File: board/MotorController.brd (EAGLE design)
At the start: 83.5 x 58.4 mm, 34 parts, among them Q1 IPP80P03P4L-04, Q2 8Mhz, T1 BT139X-600E, U1 ATTINY84-20PU

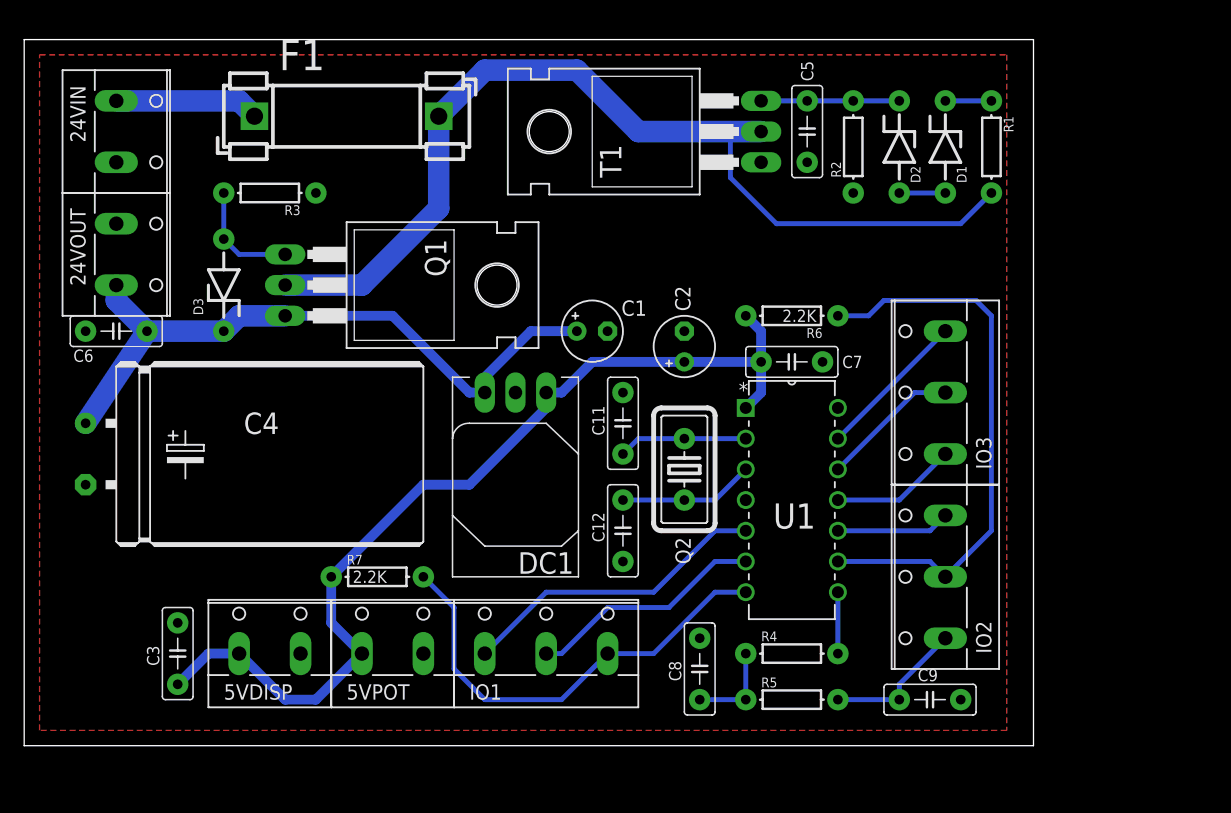
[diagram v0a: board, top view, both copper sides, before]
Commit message: Update with current design rules and current library
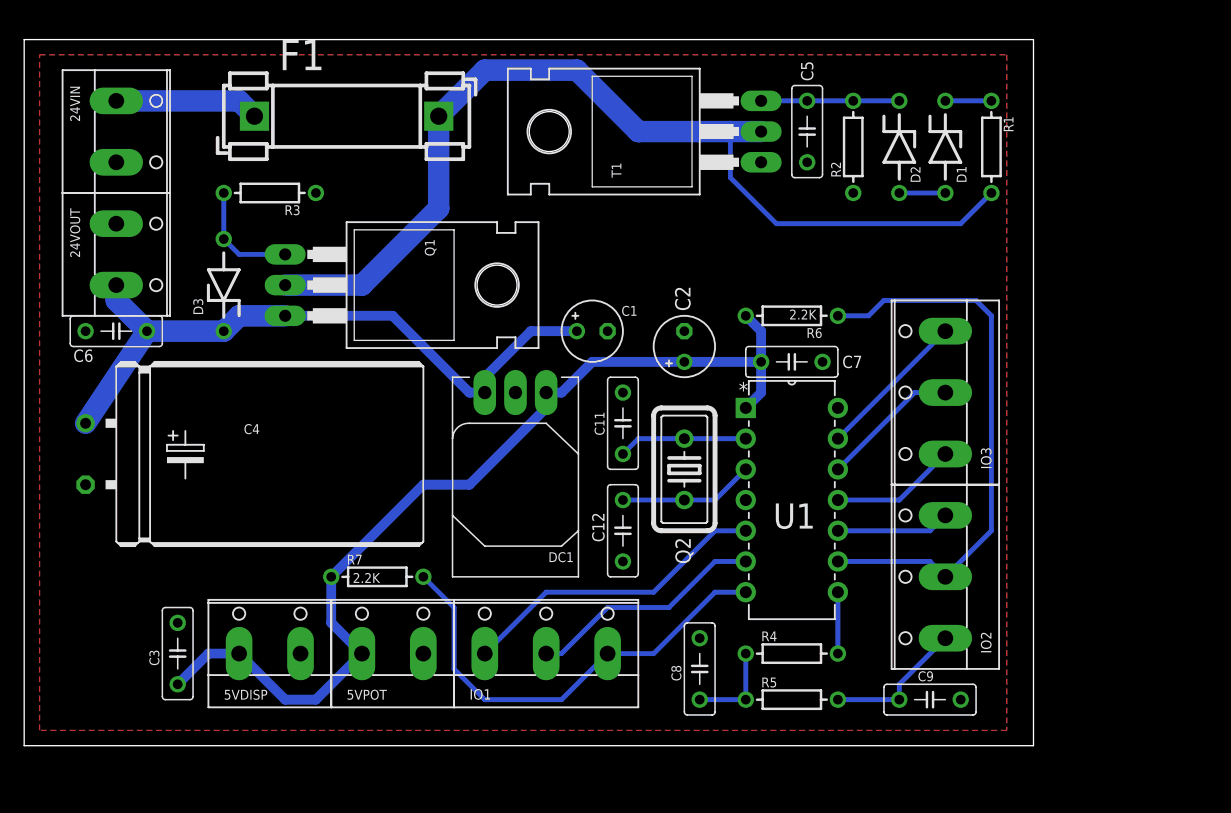
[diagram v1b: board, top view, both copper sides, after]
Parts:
- 24VIN, 24VOUT, 5VDISP, 5VPOT: value (none) -> SCREW-TERM-2
- C1, C2: device adafruit:E2,5-5 -> SaintGimp:CAP-POL-2.5-5
- F1: device fuse:FUSE_HOLDER_5X20MM -> SaintGimp:FUSE_HOLDER_5X20MM
- IO1, IO2, IO3: value (none) -> SCREW-TERM-3
- U1: device Atmel_By_element14_Batch_1:DIP254P762X533-14 -> SaintGimp:DIP14
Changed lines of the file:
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@@
 <?xml version="1.0" encoding="utf-8"?>
 <!DOCTYPE eagle SYSTEM "eagle.dtd">
-<eagle version="6.5.0">
+<eagle version="7.2.0">
 <drawing>
 <settings>
@@
 <layer number="56" name="wert" color="7" fill="1" visible="no" active="no"/>
 <layer number="57" name="tCAD" color="7" fill="1" visible="no" active="no"/>
+<layer number="90" name="Modules" color="5" fill="1" visible="no" active="no"/>
 <layer number="91" name="Nets" color="2" fill="1" visible="no" active="no"/>
 <layer number="92" name="Busses" color="1" fill="1" visible="no" active="no"/>
@@
 <layer number="97" name="Info" color="7" fill="1" visible="no" active="no"/>
 <layer number="98" name="Guide" color="6" fill="1" visible="no" active="no"/>
+<layer number="99" name="SpiceOrder" color="7" fill="1" visible="no" active="no"/>
 <layer number="100" name="Muster" color="7" fill="1" visible="no" active="no"/>
 <layer number="101" name="Patch_Top" color="12" fill="4" visible="no" active="yes"/>
@@
 <layer number="111" name="LPC17xx" color="7" fill="1" visible="yes" active="yes"/>
 <layer number="112" name="tSilk" color="7" fill="1" visible="yes" active="yes"/>
+<layer number="113" name="IDFDebug" color="7" fill="1" visible="yes" active="yes"/>
 <layer number="116" name="Patch_BOT" color="9" fill="4" visible="no" active="yes"/>
 <layer number="121" name="_tsilk" color="7" fill="1" visible="no" active="yes"/>
@@
 <layer number="223" name="223bmp" color="24" fill="1" visible="no" active="no"/>
 <layer number="224" name="224bmp" color="25" fill="1" visible="no" active="no"/>
+<layer number="225" name="225bmp" color="7" fill="1" visible="yes" active="yes"/>
+<layer number="226" name="226bmp" color="7" fill="1" visible="yes" active="yes"/>
+<layer number="227" name="227bmp" color="7" fill="1" visible="yes" active="yes"/>
+<layer number="228" name="228bmp" color="7" fill="1" visible="yes" active="yes"/>
+<layer number="229" name="229bmp" color="7" fill="1" visible="yes" active="yes"/>
+<layer number="230" name="230bmp" color="7" fill="1" visible="yes" active="yes"/>
+<layer number="231" name="231bmp" color="7" fill="1" visible="yes" active="yes"/>
 <layer number="248" name="Housing" color="7" fill="1" visible="yes" active="yes"/>
 <layer number="249" name="Edge" color="7" fill="1" visible="yes" active="yes"/>
@@
 <layer number="251" name="SMDround" color="12" fill="11" visible="no" active="no"/>
 <layer number="254" name="cooling" color="7" fill="1" visible="no" active="yes"/>
+<layer number="255" name="routoute" color="7" fill="1" visible="yes" active="yes"/>
 </layers>
 <board>
@@
 <param name="mdDrill" value="6mil"/>
 <param name="mdSmdStop" value="0mil"/>
-<param name="msWidth" value="6mil"/>
+<param name="msWidth" value="10mil"/>
 <param name="msDrill" value="13mil"/>
 <param name="msMicroVia" value="13mil"/>
 <param name="msBlindViaRatio" value="0.5"/>
-<param name="rvPadTop" value="0.25"/>
+<param name="rvPadTop" value="0.35"/>
 <param name="rvPadInner" value="0.25"/>
-<param name="rvPadBottom" value="0.25"/>
+<param name="rvPadBottom" value="0.35"/>
 <param name="rvViaOuter" value="0.25"/>
 <param name="rvViaInner" value="0.25"/>
@@
 <pass name="Default">
 <param name="RoutingGrid" value="8mil"/>
+<param name="AutoGrid" value="1"/>
+<param name="Efforts" value="0"/>
+<param name="TopRouterVariant" value="1"/>
 <param name="tpViaShape" value="round"/>
 <param name="PrefDir.1" value="0"/>
@@
 </autorouter>
 <elements>
-<element name="24VIN" library="SaintGimp" package="SCREW-TERM-2" value="" x="7.62" y="50.8" rot="R270"/>
-<element name="24VOUT" library="SaintGimp" package="SCREW-TERM-2" value="" x="7.62" y="40.64" rot="R270"/>
-<element name="5VPOT" library="SaintGimp" package="SCREW-TERM-2" value="" x="30.48" y="7.62"/>
-<element name="5VDISP" library="SaintGimp" package="SCREW-TERM-2" value="" x="20.32" y="7.62"/>
-<element name="C1" library="adafruit" package="E2,5-5" value="47uF" x="46.99" y="34.29"/>
+<element name="24VIN" library="SaintGimp" package="SCREW-TERM-2" value="SCREW-TERM-2" x="7.62" y="50.8" rot="R270"/>
+<element name="24VOUT" library="SaintGimp" package="SCREW-TERM-2" value="SCREW-TERM-2" x="7.62" y="40.64" rot="R270"/>
+<element name="5VPOT" library="SaintGimp" package="SCREW-TERM-2" value="SCREW-TERM-2" x="30.48" y="7.62"/>
+<element name="5VDISP" library="SaintGimp" package="SCREW-TERM-2" value="SCREW-TERM-2" x="20.32" y="7.62"/>
+<element name="C1" library="SaintGimp" package="CAP-POL-2.5-5" value="47uF" x="46.99" y="34.29"/>
 <element name="C4" library="SaintGimp" package="CAP-POL-25-14" value="470uF" x="22.86" y="24.13"/>
-<element name="F1" library="fuse" package="FUSE_HOLDER_5X20MM" value="FUSEBLANK_5X20MM" x="19.05" y="52.07">
-<attribute name="OC_NEWARK" value="unknown" x="19.05" y="52.07" size="1.778" layer="27" display="off"/>
-<attribute name="MPN" value="" x="19.05" y="52.07" size="1.778" layer="27" display="off"/>
-<attribute name="MF" value="" x="19.05" y="52.07" size="1.778" layer="27" display="off"/>
-<attribute name="OC_FARNELL" value="unknown" x="19.05" y="52.07" size="1.778" layer="27" display="off"/>
-</element>
+<element name="F1" library="SaintGimp" package="FUSE_HOLDER_5X20MM" value="FUSEBLANK_5X20MM" x="19.05" y="52.07"/>
 <element name="T1" library="SaintGimp" package="TO220BH" value="BT139X-600E" x="54.61" y="50.8" rot="R90"/>
 <element name="D2" library="SaintGimp" package="ZDIO-7.5" value="22V" x="72.39" y="49.53" smashed="yes" rot="R270">
@@
 </element>
 <element name="D3" library="SaintGimp" package="ZDIO-7.5" value="5.1V" x="16.51" y="38.1" rot="R90"/>
-<element name="C2" library="adafruit" package="E2,5-5" value="47uF" x="54.61" y="33.02" smashed="yes" rot="R90">
+<element name="C2" library="SaintGimp" package="CAP-POL-2.5-5" value="47uF" x="54.61" y="33.02" smashed="yes" rot="R90">
 <attribute name="NAME" x="55.118" y="35.941" size="1.27" layer="25" ratio="10" rot="R90"/>
 <attribute name="VALUE" x="57.023" y="35.433" size="1.27" layer="27" ratio="10" rot="R90"/>
@@
 <attribute name="VALUE" x="5.715" y="31.75" size="1.016" layer="27"/>
 </element>
-<element name="U1" library="Atmel_By_element14_Batch_1" package="DIP254P762X533-14" value="ATTINY84-20PU" x="67.31" y="12.7" smashed="yes">
+<element name="U1" library="SaintGimp" package="DIP14" value="ATTINY84-20PU" x="67.31" y="12.7" smashed="yes">
 <attribute name="PACKAGE" value="PDIP-14" x="41.91" y="43.18" size="1.778" layer="27" display="off"/>
 <attribute name="OC_NEWARK" value="58M3794" x="41.91" y="43.18" size="1.778" layer="27" display="off"/>
@@
 <attribute name="VALUE" value="" x="63.5" y="3.81" size="1.778" layer="27" display="off"/>
 </element>
-<element name="IO2" library="SaintGimp" package="SCREW-TERM-3" value="" x="76.2" y="13.97" rot="R90"/>
-<element name="IO3" library="SaintGimp" package="SCREW-TERM-3" value="" x="76.2" y="29.21" rot="R90"/>
-<element name="IO1" library="SaintGimp" package="SCREW-TERM-3" value="" x="43.18" y="7.62"/>
+<element name="IO2" library="SaintGimp" package="SCREW-TERM-3" value="SCREW-TERM-3" x="76.2" y="13.97" rot="R90"/>
+<element name="IO3" library="SaintGimp" package="SCREW-TERM-3" value="SCREW-TERM-3" x="76.2" y="29.21" rot="R90"/>
+<element name="IO1" library="SaintGimp" package="SCREW-TERM-3" value="SCREW-TERM-3" x="43.18" y="7.62"/>
 <element name="C8" library="SaintGimp" package="CAPACITOR-5MM" value="1uF" x="55.88" y="6.35" rot="R90"/>
 <element name="C9" library="SaintGimp" package="CAPACITOR-5MM" value="1uF" x="74.93" y="3.81"/>

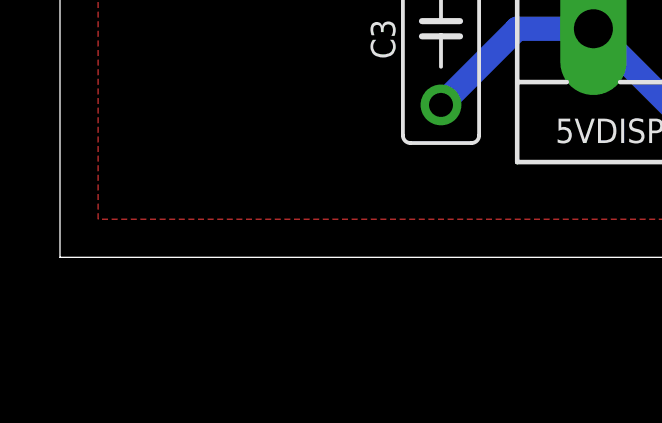
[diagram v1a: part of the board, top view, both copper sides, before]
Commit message: Pull up reset line
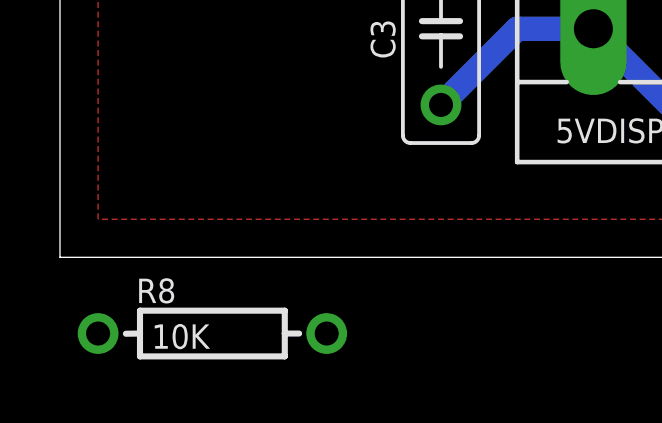
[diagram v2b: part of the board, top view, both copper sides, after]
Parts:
- added R8: 10K, SaintGimp:AXIAL-7.5MM
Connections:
- new net N$2: R8.P$2, U1.4
- new net VCC: R8.P$1
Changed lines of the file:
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@@
 <element name="R6" library="SaintGimp" package="AXIAL-7.5MM" value="2.2K" x="63.5" y="35.56" rot="R180"/>
 <element name="R7" library="SaintGimp" package="AXIAL-7.5MM" value="2.2K" x="29.21" y="13.97"/>
+<element name="R8" library="SaintGimp" package="AXIAL-7.5MM" value="10K" x="5.08" y="-2.54"/>
 </elements>
 <signals>
@@
 <wire x1="59.69" y1="3.81" x2="55.88" y2="3.81" width="0.4064" layer="16"/>
 </signal>
+<signal name="N$2">
+<contactref element="U1" pad="4"/>
+<contactref element="R8" pad="P$2"/>
+<wire x1="8.89" y1="-2.54" x2="59.69" y2="20.32" width="0" layer="19" extent="1-1"/>
+</signal>
+<signal name="VCC">
+<contactref element="R8" pad="P$1"/>
+</signal>
 </signals>

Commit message: New board layout
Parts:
- removed 5VDISP, 5VPOT: SCREW-TERM-2, SaintGimp:SCREW-TERM-2
- removed IO1, IO2, IO3: SCREW-TERM-3, SaintGimp:SCREW-TERM-3
- removed R7: 2.2K, SaintGimp:AXIAL-7.5MM
- added C10: 0.1uF, SaintGimp:CAPACITOR-5MM
- added CNTRL: SCREW-TERM-2, SaintGimp:SCREW-TERM-2
- added DISP, MOTOR, RAMP, SPD: SCREW-TERM-3, SaintGimp:SCREW-TERM-3
- added U$1, U$2, U$3, U$4: (no value), holes:4,1
- C11, C12: device SaintGimp:CAPACITOR-5MM -> SaintGimp:CAPACITOR-2.5MM
- C6: value 0.1uF -> 1uF
- F1: value FUSEBLANK_5X20MM -> 4A
- R1, R2: value 1K -> (none)
- R3, R8: value 10K -> (none)
- R4, R5: value 220 -> (none)
- R6: value 2.2K -> (none)
- moved 24VOUT 83.9 mm to (90.2, 25.4), turned to 90 degrees
- moved C6 74.9 mm to (82.5, 34.3), turned to 270 degrees
- moved C4 56.1 mm to (77.5, 11.4), turned to 270 degrees
- moved C3 55.4 mm to (64.8, 26.7), turned to 180 degrees
- moved R1 49.8 mm to (63.5, 2.54), turned to 180 degrees
- moved C7 48.4 mm to (15.2, 35.6), turned to 270 degrees
- moved F1 47.1 mm to (21.6, 5.08)
- moved D1 45.0 mm to (63.5, 6.35), turned to 180 degrees
- moved T1 44.7 mm to (49.5, 6.35)
- moved C9 43.1 mm to (45.7, 35.6), turned to 270 degrees
- moved R8 43.1 mm to (36.8, 26.7), turned to 180 degrees
- moved U1 42.4 mm to (34.3, 39.4), turned to 90 degrees
- moved D2 40.4 mm to (63.5, 10.2), turned to 180 degrees
- moved R6 38.6 mm to (25.4, 41.9), turned to 0 degrees
- moved R4 37.8 mm to (38.1, 35.6), turned to 90 degrees
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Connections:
- removed net 5V: 5VDISP.1, 5VPOT.1, C2.+, C3.1, C7.2, DC1.P3, R6.P$2, R7.P$1, U1.1
- removed net I2C_SCL: IO2.2, R6.P$1, U1.9
- removed net I2C_SDA: IO1.3, R7.P$2, U1.7
- new net N$8: DISP.3, R6.P$1
- new net SERIAL_TX: R6.P$2, U1.7
- net 24V-PROTECTED: now also C10.2
- net DIR_IN: now also CNTRL.1; no longer IO3.1
- net DIR_OUT: now also MOTOR.3; no longer IO1.2
- net GND: now also C10.1, DISP.2, RAMP.2, SPD.2; no longer 5VDISP.2, 5VPOT.2
- net N$10: now also MOTOR.1; no longer IO2.1
- net RAMP_IN: now also RAMP.3; no longer IO3.2
- net RPM_IN: now also MOTOR.2; no longer IO1.1
- net SPD_IN: now also SPD.3; no longer IO3.3
- net START_IN: now also CNTRL.2; no longer IO2.3
- net VCC: now also C2.+, C3.1, C7.2, DC1.P3, DISP.1, RAMP.1, SPD.1, U1.1
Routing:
- net VCC: track 0.00 -> 109.8 mm
- net 5V: track 79.2 -> 0.00 mm
- net N$10: track 11.7 -> 68.1 mm, vias 0 -> 2
- net I2C_SCL: track 46.3 -> 0.00 mm
- net DIR_OUT: track 19.7 -> 64.2 mm, vias 0 -> 2
- net RPM_IN: track 25.8 -> 68.4 mm, vias 0 -> 2
- net I2C_SDA: track 37.5 -> 0.00 mm
- net 24V: track 81.3 -> 48.1 mm
- net 24V-PROTECTED: track 55.6 -> 80.0 mm
- net START_IN: track 9.42 -> 24.2 mm, vias 0 -> 2
- net RAMP_IN: track 11.5 -> 26.3 mm
- net DIR_IN: track 10.5 -> 24.1 mm
- net SERIAL_TX: track 0.00 -> 12.3 mm
- net N$7: track 11.4 -> 21.3 mm
- net N$2: track 0.00 -> 9.34 mm
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- added copper zone on layer 16, net GND
- removed copper zone on layer 1, net GND
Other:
- board size 83.5 x 58.4 mm -> 97.8 x 55.9 mm
